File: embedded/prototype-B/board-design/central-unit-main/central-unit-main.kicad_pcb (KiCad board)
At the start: 2 copper layers, 45 x 92.5 mm, 101 parts, among them IC1 VEML6030, J1 Screw_Terminal_01x02, J2 2171790001, J3 Conn_02x05_Odd_Even, J4 Conn_ARM_JTAG_SWD_20, SW1 CAS-120TA1, U1 STM32L452RETx, U2 TPS63000, U3 MIC2778-2YM5-TR, U4 USBLC6-2SC6, U5 BQ24074RGT, U6 LIS2HH12, Y1 ECS-_327-12_5-34B-TR, Y2 STDCSU1-8M

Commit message: [Central unit] Redesign the power lines
Changed the battery charger footprint to a version with thermal vias.
Updated BOM.

Signed-off-by: Nicolae-Andrei Prodan <vasilenicolaeandrei@gmail.com>
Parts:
- U5: footprint Package_DFN_QFN:VQFN-16-1EP_3x3mm_P0.5mm_EP1.6x1.6mm -> Package_DFN_QFN:VQFN-16-1EP_3x3mm_P0.5mm_EP1.6x1.6mm_ThermalVias
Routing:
- net GND: vias 47 -> 46
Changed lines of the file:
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@@
 		(capping no)
 		(filling no)
-		(zone_defaults)
 		(pcbplotparams
 			(layerselection 0x00000000_00000000_55555555_5755f5ff)
@@
 		)
 	)
-	(footprint "Package_DFN_QFN:VQFN-16-1EP_3x3mm_P0.5mm_EP1.6x1.6mm"
+	(footprint "Package_DFN_QFN:VQFN-16-1EP_3x3mm_P0.5mm_EP1.6x1.6mm_ThermalVias"
 		(locked yes)
 		(layer "F.Cu")
@@
 		(tags "VQFN NoLead")
 		(property "Reference" "U5"
-			(at -2.5 3 0)
+			(at -3 0.5 0)
 			(layer "F.SilkS")
 			(effects
@@
 		)
 		(property "Value" "BQ24074RGT"
-			(at 0 2.83 90)
+			(at 0 2.83 270)
 			(layer "F.Fab")
 			(effects
@@
 		)
 		(property "Datasheet" "http://www.ti.com/lit/ds/symlink/bq24074.pdf"
-			(at 0 0 90)
+			(at 0 0 270)
 			(layer "F.Fab")
 			(hide yes)
@@
 		)
 		(property "Description" "USB-Friendly Li-Ion Battery Charger and Power-Path Management, VQFN-16"
-			(at 0 0 90)
+			(at 0 0 270)
 			(layer "F.Fab")
 			(hide yes)
@@
 		)
 		(fp_text user "${REFERENCE}"
-			(at 0 0 90)
+			(at 0 0 270)
 			(layer "F.Fab")
 			(effects
@@
 		(pad "" smd roundrect
 			(at -0.4 -0.4 270)
-			(size 0.64 0.64)
+			(size 0.69 0.69)
 			(layers "F.Paste")
 			(roundrect_rratio 0.25)
@@
 		(pad "" smd roundrect
 			(at -0.4 0.4 270)
-			(size 0.64 0.64)
+			(size 0.69 0.69)
 			(layers "F.Paste")
 			(roundrect_rratio 0.25)
@@
 		(pad "" smd roundrect
 			(at 0.4 -0.4 270)
-			(size 0.64 0.64)
+			(size 0.69 0.69)
 			(layers "F.Paste")
 			(roundrect_rratio 0.25)
@@
 		(pad "" smd roundrect
 			(at 0.4 0.4 270)
-			(size 0.64 0.64)
+			(size 0.69 0.69)
 			(layers "F.Paste")
 			(roundrect_rratio 0.25)
@@
 			(pintype "passive")
 		)
+		(pad "17" thru_hole circle
+			(at -0.55 -0.55 270)
+			(size 0.5 0.5)
+			(drill 0.2)
+			(property pad_prop_heatsink)
+			(layers "*.Cu")
+			(remove_unused_layers no)
+			(net "GND")
+			(pinfunction "VSS_17")
+			(pintype "passive")
+		)
+		(pad "17" thru_hole circle
+			(at -0.55 0.55 270)
+			(size 0.5 0.5)
+			(drill 0.2)
+			(property pad_prop_heatsink)
+			(layers "*.Cu")
+			(remove_unused_layers no)
+			(net "GND")
+			(pinfunction "VSS_17")
+			(pintype "passive")
+		)
 		(pad "17" smd rect
 			(at 0 0 270)
@@
 			(zone_connect 2)
 		)
+		(pad "17" smd rect
+			(at 0 0 270)
+			(size 1.6 1.6)
+			(property pad_prop_heatsink)
+			(layers "B.Cu")
+			(net "GND")
+			(pinfunction "VSS_17")
+			(pintype "passive")
+			(zone_connect 2)
+		)
+		(pad "17" thru_hole circle
+			(at 0.55 -0.55 270)
+			(size 0.5 0.5)
+			(drill 0.2)
+			(property pad_prop_heatsink)
+			(layers "*.Cu")
+			(remove_unused_layers no)
+			(net "GND")
+			(pinfunction "VSS_17")
+			(pintype "passive")
+		)
+		(pad "17" thru_hole circle
+			(at 0.55 0.55 270)
+			(size 0.5 0.5)
+			(drill 0.2)
+			(property pad_prop_heatsink)
+			(layers "*.Cu")
+			(remove_unused_layers no)
+			(net "GND")
+			(pinfunction "VSS_17")
+			(pintype "passive")
+		)
 		(embedded_fonts no)
 		(model "${KICAD10_3DMODEL_DIR}/Package_DFN_QFN.3dshapes/VQFN-16-1EP_3x3mm_P0.5mm_EP1.6x1.6mm.step"
@@
 	)
 	(via
-		(at 138 59)
-		(size 0.61)
-		(drill 0.3)
-		(layers "F.Cu" "B.Cu")
-		(locked yes)
-		(net "GND")
-	)
-	(via
 		(at 151.5 100)
 		(size 0.61)
@@
 		(end 141.25 119.5)
 		(width 0.254)
+		(locked yes)
 		(layer "F.Cu")
 		(net "/MCU/I2C1_SCL")
@@
 		(end 141.2375 119.5125)
 		(width 0.254)
+		(locked yes)
 		(layer "F.Cu")
 		(net "/MCU/I2C1_SCL")
@@
 		(end 142 116.5)
 		(width 0.254)
+		(locked yes)
 		(layer "F.Cu")
 		(net "/MCU/I2C1_SCL")
@@
 		(drill 0.3)
 		(layers "F.Cu" "B.Cu")
+		(locked yes)
 		(net "/MCU/I2C1_SCL")
 	)
@@
 		(drill 0.3)
 		(layers "F.Cu" "B.Cu")
+		(locked yes)
 		(net "/MCU/I2C1_SCL")
 	)

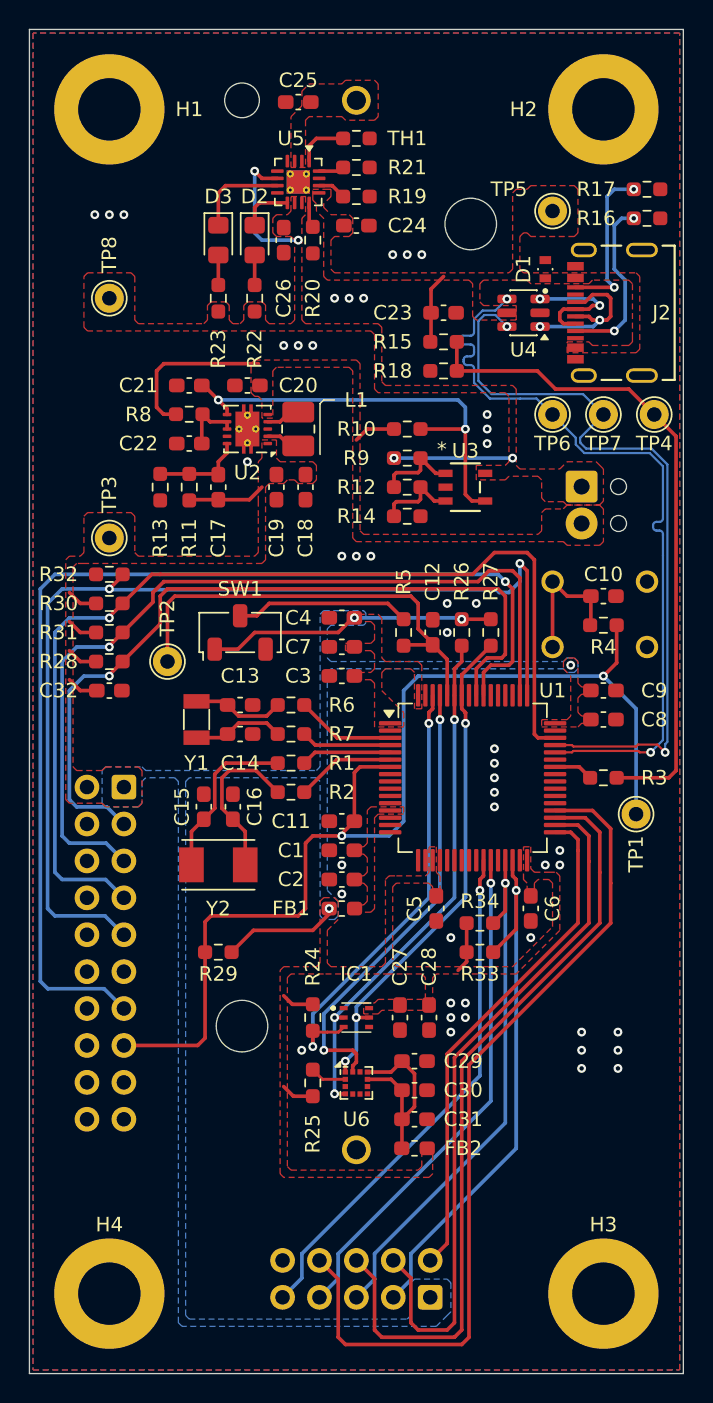
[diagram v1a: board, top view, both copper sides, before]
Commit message: [All] Enhance BOM
Added the PCBWay required fields in central unit BOM for assembly
feature. Removed the jumper resistors for the crystals as well.

Signed-off-by: Nicolae-Andrei Prodan <vasilenicolaeandrei@gmail.com>
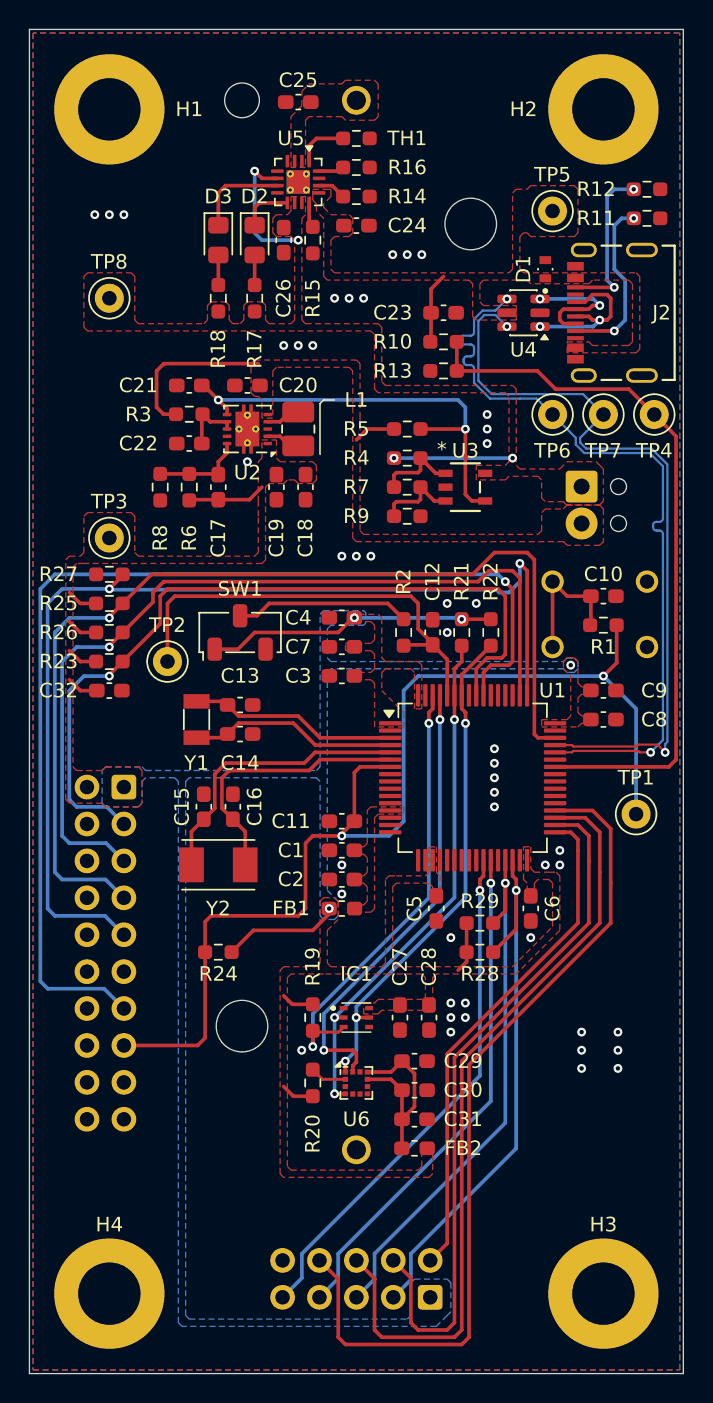
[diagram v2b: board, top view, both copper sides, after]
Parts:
- removed the R1 at (137.5, 99.0)
- removed the R2 at (137.5, 101.0)
- removed the R3 at (159.0, 100.0)
- removed the R6 at (137.5, 95.0)
- removed the R7 at (137.5, 97.0)
- C1, C12, C21, C22, C27, C29, C30, C5, C6, C7, C8: value 100nF/6.3V/20%/C0603 -> 100nF/16V/10%/C0603
- C10, C15, C16: value 10pF/6.3V/20%/C0603 -> 10pF/16V/10%/C0603
- C11: value 22nF/6.3V/20%/C0603 -> 22nF/16V/10%/C0603
- C13, C14: value 18pF/6.3V/20%/C0603 -> 18pF/16V/10%/C0603
- C17: value 2.2pF/6.3V/20%/C0603 -> 2.2pF/16V/+\-0.1pF/C0603
- C18: value 22uF/6.3V/20%/C0603 -> 22uF/16V/20%/C0603
- C19, C20, C23, C24, C25, C26, C28, C31, C32, C4: value 10uF/6.3V/20%/C0603 -> 10uF/16V/10%/C0603
- C2, C3, C9: value 1uF/6.3V/20%/C0603 -> 1uF/16V/10%/C0603
- FB1, FB2: value BLM18PG121SN1D -> 120R @ 100MHz
- L1: value 2.2uH(MAMK2520T2R2M) -> 2.2uH
- R1: renamed from R4; value 1K/R0603 -> 1K/0.1W/1%/R0603
- R10: renamed from R15; value 33K/R0603 -> 33K/0.1W/1%/R0603
- R11: renamed from R16; value 5.1K/R0603 -> 5.1K/0.1W/1%/R0603
- R12: renamed from R17; value 5.1K/R0603 -> 5.1K/0.1W/1%/R0603
- R13: renamed from R18; value 82K/R0603 -> 82K/0.1W/1%/R0603
- R14: renamed from R19; value 68K/R0603 -> 68K/0.1W/1%/R0603
- R15: renamed from R20; value 3.48K/R0603 -> 3.48K/0.1W/1%/R0603
- R16: renamed from R21; value 2.21K/R0603 -> 2.21K/0.1W/1%/R0603
- R17: renamed from R22; value 1.5K/R0603 -> 1.5K/0.1W/1%/R0603
- R18: renamed from R23; value 1.5K/R0603 -> 1.5K/0.1W/1%/R0603
- R19: renamed from R24; value 10K/R0603 -> 10K/0.1W/1%/R0603
- R2: renamed from R5; value 10K/R0603 -> 10K/0.1W/1%/R0603
- R20: renamed from R25; value 10K/R0603 -> 10K/0.1W/1%/R0603
- R21: renamed from R26; value 10K/R0603 -> 10K/0.1W/1%/R0603
- R22: renamed from R27; value 10K/R0603 -> 10K/0.1W/1%/R0603
- R23: renamed from R28; value 10K/R0603 -> 10K/0.1W/1%/R0603
- R24: renamed from R29; value 10K/R0603 -> 10K/0.1W/1%/R0603
- R25: renamed from R30; value 10K/R0603 -> 10K/0.1W/1%/R0603
- R26: renamed from R31; value 10K/R0603 -> 10K/0.1W/1%/R0603
- R27: renamed from R32; value 10K/R0603 -> 10K/0.1W/1%/R0603
- R28: renamed from R33; value 4.7K/R0603 -> 4.7K/0.1W/1%/R0603
- R29: renamed from R34; value 4.7K/R0603 -> 4.7K/0.1W/1%/R0603
- R3: renamed from R8; value 100R/R0603 -> 100R/0.1W/1%/R0603
- R4: renamed from R9; value 604K/R0603 -> 604K/0.1W/1%/R0603
- R5: renamed from R10; value 100K/R0603 -> 100K/0.1W/1%/R0603
- R6: renamed from R11; value 1M/R0603 -> 1M/0.1W/1%/R0603
- R7: renamed from R12; value 56K/R0603 -> 56K/0.1W/1%/R0603
- R8: renamed from R13; value 178K/R0603 -> 178K/0.1W/1%/R0603
- R9: renamed from R14; value 340K/R0603 -> 340K/0.1W/1%/R0603
- TP1, TP2, TP3, TP4, TP5, TP6, TP7, TP8: footprint TestPoint:TestPoint_THTPad_D2.0mm_Drill1.0mm -> TestPoint:TestPoint_Keystone_5000-5004_Miniature
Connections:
- U1 pad 3: Net-(U1-PC14) -> /MCU/OSC_32K_IN
- U1 pad 4: Net-(U1-PC15) -> /MCU/OSC_32K_OUT
- U1 pad 42: Net-(U1-PA9) -> /MCU/USB_DETECT
- U1 pad 5: Net-(U1-PH0) -> /MCU/OSC_8M_IN
- U1 pad 6: Net-(U1-PH1) -> /MCU/OSC_8M_OUT
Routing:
- net /MCU/OSC_32K_OUT: track 6.32 -> 14.4 mm
- net /MCU/OSC_32K_IN: track 6.32 -> 14.4 mm
- net /MCU/OSC_8M_IN: track 11.6 -> 19.6 mm
- net /MCU/OSC_8M_OUT: track 11.3 -> 18.7 mm
- net Net-(U1-PC14): track 6.85 -> 0.00 mm
- net Net-(U1-PH1): track 6.84 -> 0.00 mm
- net Net-(U1-PC15): track 6.23 -> 0.00 mm
- net Net-(U1-PH0): track 6.22 -> 0.00 mm
- net /MCU/USB_DETECT: track 46.2 -> 49.7 mm
- net Net-(U1-PA9): track 2.72 -> 0.00 mm

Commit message: [All] Enhance BOM
Fixed BOM issues. Added ERC and DRC reports.

Signed-off-by: Nicolae-Andrei Prodan <vasilenicolaeandrei@gmail.com>
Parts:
- D2: value LED -> LED RED
- D3: value LED -> LED GREEN
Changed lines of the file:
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@@
 			)
 		)
-		(property "Value" "LED"
+		(property "Value" "LED GREEN"
 			(at 0 1.65 90)
 			(layer "F.Fab")
@@
 			)
 		)
-		(property "MPN" "RES 178K OHM 1% 1/10W 0603"
+		(property "MPN" "RC0603FR-13178KL"
 			(at 0 0 270)
 			(unlocked yes)
@@
 			)
 		)
-		(attr smd dnp)
+		(attr smd exclude_from_pos_files dnp)
 		(duplicate_pad_numbers_are_jumpers no)
 		(fp_line
@@
 			)
 		)
-		(property "Value" "LED"
+		(property "Value" "LED RED"
 			(at 0 1.65 90)
 			(layer "F.Fab")
@@
 	)
 	(segment
-		(start 130.65 105.99)
-		(end 130.65 103.7025)
-		(width 0.254)
-		(locked yes)
-		(layer "F.Cu")
-		(net "/MCU/OSC_8M_IN")
-	)
-	(segment
-		(start 132.2544 99.7456)
-		(end 133.01 98.99)
-		(width 0.254)
-		(locked yes)
-		(layer "F.Cu")
-		(net "/MCU/OSC_8M_IN")
-	)
-	(segment
-		(start 133.01 98.99)
-		(end 138.4125 98.99)
-		(width 0.254)
-		(locked yes)
-		(layer "F.Cu")
-		(net "/MCU/OSC_8M_IN")
-	)
-	(segment
-		(start 139.1525 98.25)
-		(end 144.325 98.25)
-		(width 0.254)
-		(locked yes)
-		(layer "F.Cu")
-		(net "/MCU/OSC_8M_IN")
-	)
-	(segment
-		(start 131.5 102.8525)
-		(end 132.2544 102.0981)
-		(width 0.254)
-		(locked yes)
-		(layer "F.Cu")
-		(net "/MCU/OSC_8M_IN")
-	)
-	(segment
-		(start 132.2544 102.0981)
-		(end 132.2544 99.7456)
-		(width 0.254)
-		(locked yes)
-		(layer "F.Cu")
-		(net "/MCU/OSC_8M_IN")
-	)
-	(segment
-		(start 130.65 103.7025)
-		(end 131.5 102.8525)
-		(width 0.254)
-		(locked yes)
-		(layer "F.Cu")
-		(net "/MCU/OSC_8M_IN")
-	)
-	(segment
-		(start 138.4125 98.99)
-		(end 139.1525 98.25)
-		(width 0.254)
-		(locked yes)
-		(layer "F.Cu")
-		(net "/MCU/OSC_8M_IN")
-	)
-	(segment
 		(start 138.75 56.5)
 		(end 139.25 56)
@@
 	)
 	(segment
-		(start 133.8919 96.2356)
-		(end 137.6581 96.2356)
-		(width 0.254)
-		(locked yes)
-		(layer "F.Cu")
-		(net "/MCU/OSC_32K_OUT")
-	)
-	(segment
-		(start 137.6581 96.2356)
-		(end 139.1725 97.75)
-		(width 0.254)
-		(locked yes)
-		(layer "F.Cu")
-		(net "/MCU/OSC_32K_OUT")
-	)
-	(segment
-		(start 132.8875 97.24)
-		(end 133.1375 96.99)
-		(width 0.254)
-		(locked yes)
-		(layer "F.Cu")
-		(net "/MCU/OSC_32K_OUT")
-	)
-	(segment
-		(start 131 97.24)
-		(end 132.8875 97.24)
-		(width 0.254)
-		(locked yes)
-		(layer "F.Cu")
-		(net "/MCU/OSC_32K_OUT")
-	)
-	(segment
-		(start 133.1375 96.99)
-		(end 133.8919 96.2356)
-		(width 0.254)
-		(locked yes)
-		(layer "F.Cu")
-		(net "/MCU/OSC_32K_OUT")
-	)
-	(segment
-		(start 139.1725 97.75)
-		(end 144.325 97.75)
-		(width 0.254)
-		(locked yes)
-		(layer "F.Cu")
-		(net "/MCU/OSC_32K_OUT")
-	)
-	(segment
 		(start 157.075 69.25)
 		(end 159.75 69.25)
@@
 	)
 	(segment
-		(start 154.45625 72)
-		(end 155.70625 73.25)
-		(width 0.254)
-		(locked yes)
-		(layer "F.Cu")
-		(net "/MCU/USB_DETECT")
-	)
-	(segment
-		(start 164 76.5)
-		(end 162.5 75)
-		(width 0.254)
-		(locked yes)
-		(layer "F.Cu")
-		(net "/MCU/USB_DETECT")
-	)
-	(segment
-		(start 148.9125 70)
-		(end 148.9125 72)
-		(width 0.254)
-		(locked yes)
-		(layer "F.Cu")
-		(net "/MCU/USB_DETECT")
-	)
-	(segment
-		(start 164 98.75)
-		(end 164 76.5)
-		(width 0.254)
-		(locked yes)
-		(layer "F.Cu")
-		(net "/MCU/USB_DETECT")
-	)
-	(segment
-		(start 148.9125 72)
-		(end 154.45625 72)
-		(width 0.254)
-		(locked yes)
-		(layer "F.Cu")
-		(net "/MCU/USB_DETECT")
-	)
-	(segment
-		(start 163.5 99.25)
-		(end 164 98.75)
-		(width 0.254)
-		(locked yes)
-		(layer "F.Cu")
-		(net "/MCU/USB_DETECT")
-	)
-	(segment
-		(start 160.75 73.25)
-		(end 162.5 75)
-		(width 0.254)
-		(locked yes)
-		(layer "F.Cu")
-		(net "/MCU/USB_DETECT")
-	)
-	(segment
-		(start 155.70625 73.25)
-		(end 160.75 73.25)
-		(width 0.254)
-		(locked yes)
-		(layer "F.Cu")
-		(net "/MCU/USB_DETECT")
-	)
-	(segment
-		(start 155.675 99.25)
-		(end 163.5 99.25)
-		(width 0.254)
-		(locked yes)
-		(layer "F.Cu")
-		(net "/MCU/USB_DETECT")
-	)
-	(segment
 		(start 146.4125 80)
 		(end 146.4125 80.8375)
@@
 	)
 	(segment
+		(start 130.65 105.99)
+		(end 130.65 103.7025)
+		(width 0.254)
+		(locked yes)
+		(layer "F.Cu")
+		(net "/MCU/OSC_8M_IN")
+	)
+	(segment
+		(start 132.2544 99.7456)
+		(end 133.01 98.99)
+		(width 0.254)
+		(locked yes)
+		(layer "F.Cu")
+		(net "/MCU/OSC_8M_IN")
+	)
+	(segment
+		(start 133.01 98.99)
+		(end 138.4125 98.99)
+		(width 0.254)
+		(locked yes)
+		(layer "F.Cu")
+		(net "/MCU/OSC_8M_IN")
+	)
+	(segment
+		(start 139.1525 98.25)
+		(end 144.325 98.25)
+		(width 0.254)
+		(locked yes)
+		(layer "F.Cu")
+		(net "/MCU/OSC_8M_IN")
+	)
+	(segment
+		(start 131.5 102.8525)
+		(end 132.2544 102.0981)
+		(width 0.254)
+		(locked yes)
+		(layer "F.Cu")
+		(net "/MCU/OSC_8M_IN")
+	)
+	(segment
+		(start 132.2544 102.0981)
+		(end 132.2544 99.7456)
+		(width 0.254)
+		(locked yes)
+		(layer "F.Cu")
+		(net "/MCU/OSC_8M_IN")
+	)
+	(segment
+		(start 130.65 103.7025)
+		(end 131.5 102.8525)
+		(width 0.254)
+		(locked yes)
+		(layer "F.Cu")
+		(net "/MCU/OSC_8M_IN")
+	)
+	(segment
+		(start 138.4125 98.99)
+		(end 139.1525 98.25)
+		(width 0.254)
+		(locked yes)
+		(layer "F.Cu")
+		(net "/MCU/OSC_8M_IN")
+	)
+	(segment
+		(start 154.45625 72)
+		(end 155.70625 73.25)
+		(width 0.254)
+		(locked yes)
+		(layer "F.Cu")
+		(net "/MCU/USB_DETECT")
+	)
+	(segment
+		(start 164 76.5)
+		(end 162.5 75)
+		(width 0.254)
+		(locked yes)
+		(layer "F.Cu")
+		(net "/MCU/USB_DETECT")
+	)
+	(segment
+		(start 148.9125 70)
+		(end 148.9125 72)
+		(width 0.254)
+		(locked yes)
+		(layer "F.Cu")
+		(net "/MCU/USB_DETECT")
+	)
+	(segment
+		(start 164 98.75)
+		(end 164 76.5)
+		(width 0.254)
+		(locked yes)
+		(layer "F.Cu")
+		(net "/MCU/USB_DETECT")
+	)
+	(segment
+		(start 148.9125 72)
+		(end 154.45625 72)
+		(width 0.254)
+		(locked yes)
+		(layer "F.Cu")
+		(net "/MCU/USB_DETECT")
+	)
+	(segment
+		(start 163.5 99.25)
+		(end 164 98.75)
+		(width 0.254)
+		(locked yes)
+		(layer "F.Cu")
+		(net "/MCU/USB_DETECT")
+	)
+	(segment
+		(start 160.75 73.25)
+		(end 162.5 75)
+		(width 0.254)
+		(locked yes)
+		(layer "F.Cu")
+		(net "/MCU/USB_DETECT")
+	)
+	(segment
+		(start 155.70625 73.25)
+		(end 160.75 73.25)
+		(width 0.254)
+		(locked yes)
+		(layer "F.Cu")
+		(net "/MCU/USB_DETECT")
+	)
+	(segment
+		(start 155.675 99.25)
+		(end 163.5 99.25)
+		(width 0.254)
+		(locked yes)
+		(layer "F.Cu")
+		(net "/MCU/USB_DETECT")
+	)
+	(segment
 		(start 135 66.0875)
 		(end 135 64.025)
@@
 	)
 	(segment
+		(start 133.8919 96.2356)
+		(end 137.6581 96.2356)
+		(width 0.254)
+		(locked yes)
+		(layer "F.Cu")
+		(net "/MCU/OSC_32K_OUT")
+	)
+	(segment
+		(start 137.6581 96.2356)
+		(end 139.1725 97.75)
+		(width 0.254)
+		(locked yes)
+		(layer "F.Cu")
+		(net "/MCU/OSC_32K_OUT")
+	)
+	(segment
+		(start 132.8875 97.24)
+		(end 133.1375 96.99)
+		(width 0.254)
+		(locked yes)
+		(layer "F.Cu")
+		(net "/MCU/OSC_32K_OUT")
+	)
+	(segment
+		(start 131 97.24)
+		(end 132.8875 97.24)
+		(width 0.254)
+		(locked yes)
+		(layer "F.Cu")
+		(net "/MCU/OSC_32K_OUT")
+	)
+	(segment
+		(start 133.1375 96.99)
+		(end 133.8919 96.2356)
+		(width 0.254)
+		(locked yes)
+		(layer "F.Cu")
+		(net "/MCU/OSC_32K_OUT")
+	)
+	(segment
+		(start 139.1725 97.75)
+		(end 144.325 97.75)
+		(width 0.254)
+		(locked yes)
+		(layer "F.Cu")
+		(net "/MCU/OSC_32K_OUT")
+	)
+	(segment
